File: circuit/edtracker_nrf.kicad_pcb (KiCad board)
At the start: 2 copper layers, 16 parts, among them M1 NRF24LE1_MODULE_SMALL, Q1 TPS1101D, SW1 SW_PUSH_4PIN, U1 NRF24LE1_PROG, U2 MPU-6050, U3 UART_CONN

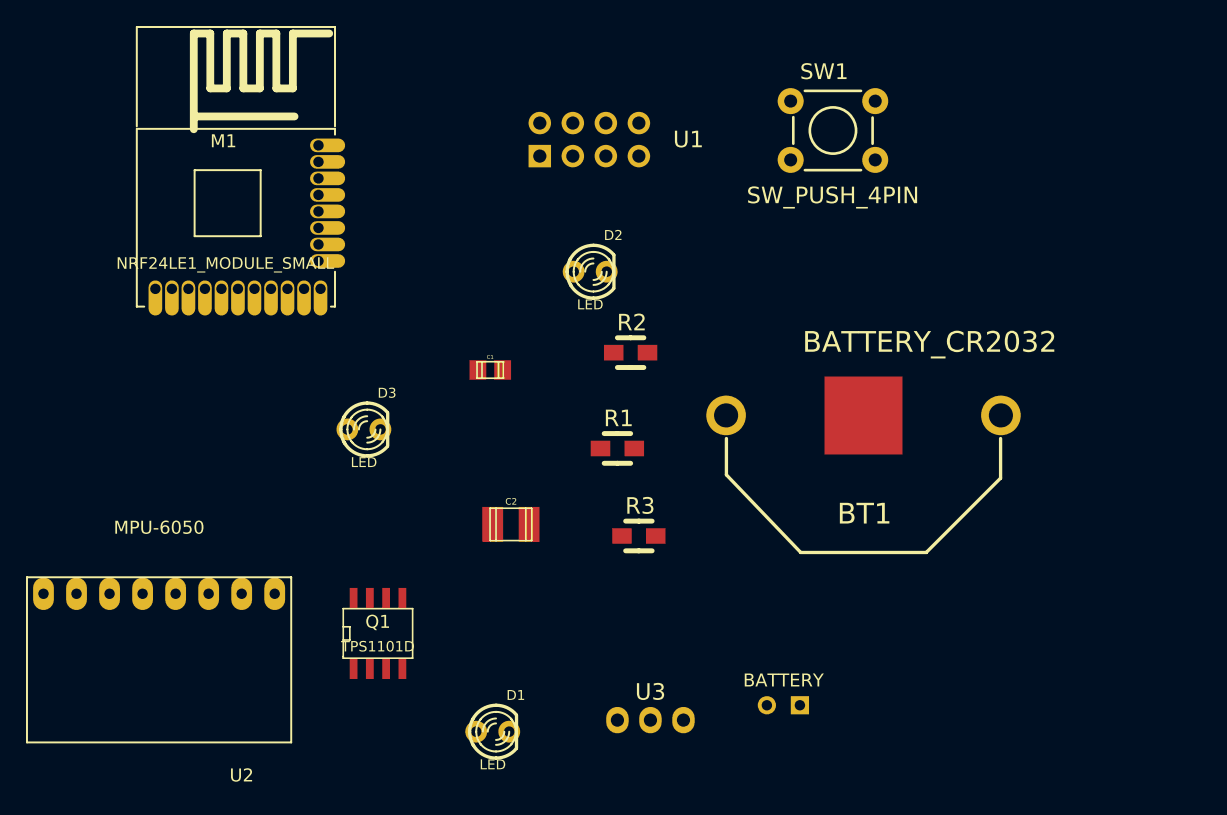
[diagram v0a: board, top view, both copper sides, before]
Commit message: 
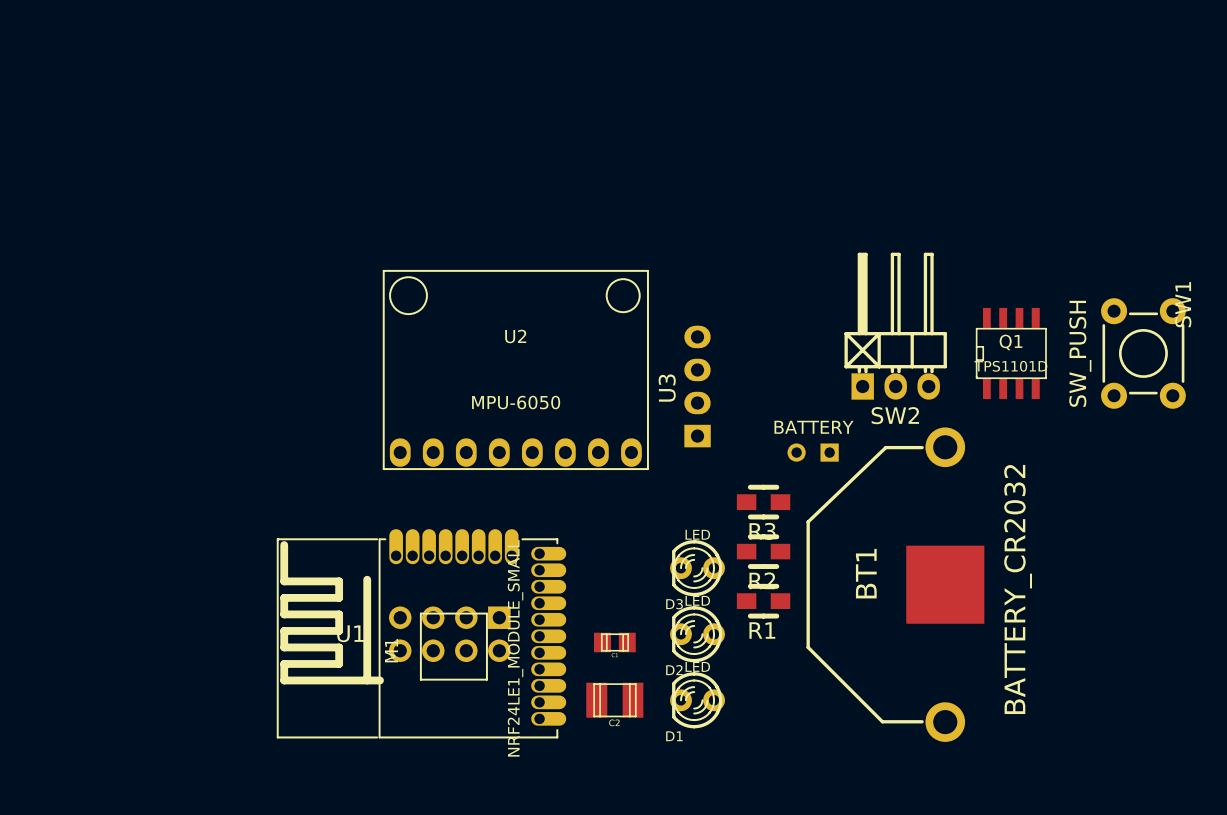
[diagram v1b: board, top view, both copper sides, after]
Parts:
- added SW2: SWITCH_INV, Pin_Headers:Pin_Header_Angled_1x03, F.Cu at (177.8, 100.3)
- SW1: value SW_PUSH_4PIN -> SW_PUSH
- U3: footprint edtracker_nrf:Pin_Header_Angled_1x03 -> edtracker_nrf:Pin_Header_1x04
- moved Q1 53.2 mm to (186.7, 97.8)
- moved U1 39.5 mm to (143.5, 119.4), turned to 180 degrees
- moved M1 36.6 mm to (144.8, 119.4), turned to 90 degrees
- moved U2 35.3 mm to (148.6, 99.1), turned to 180 degrees
- moved SW1 29.4 mm to (196.8, 97.8), turned to 270 degrees
- moved D2 29.1 mm to (162.6, 119.4), turned to 180 degrees
- moved D3 27.8 mm to (162.6, 114.3), turned to 180 degrees
- moved U3 25.9 mm to (162.6, 100.3), turned to 90 degrees
- moved C1 23.0 mm to (156.2, 120.0), turned to 180 degrees
- moved BT2 19.6 mm to (171.4, 105.4)
- moved R2 18.4 mm to (167.6, 113.0), turned to 180 degrees
- moved R1 16.3 mm to (167.6, 116.8), turned to 180 degrees
- moved D1 15.9 mm to (162.6, 124.5), turned to 180 degrees
- moved C2 15.7 mm to (156.2, 124.5), turned to 180 degrees
- moved BT1 14.5 mm to (181.6, 115.6), turned to 270 degrees
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
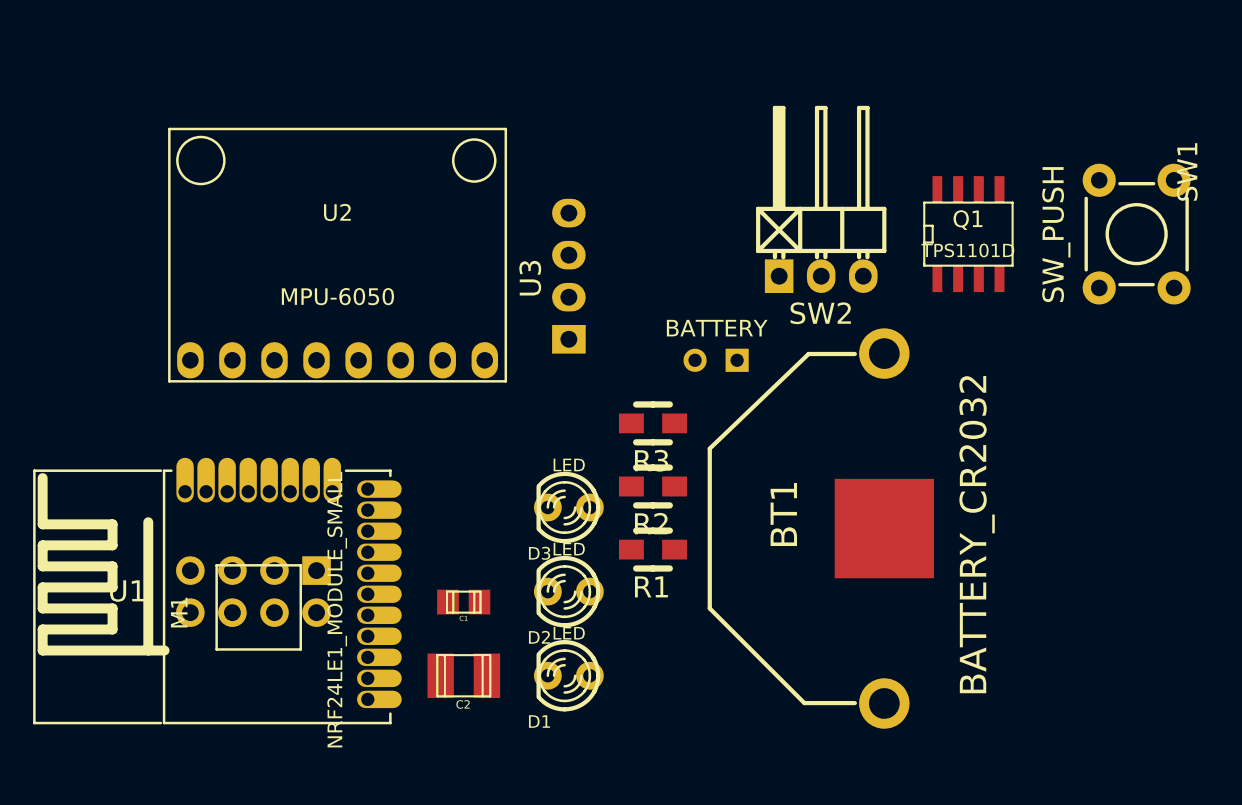
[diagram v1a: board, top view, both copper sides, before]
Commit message: 
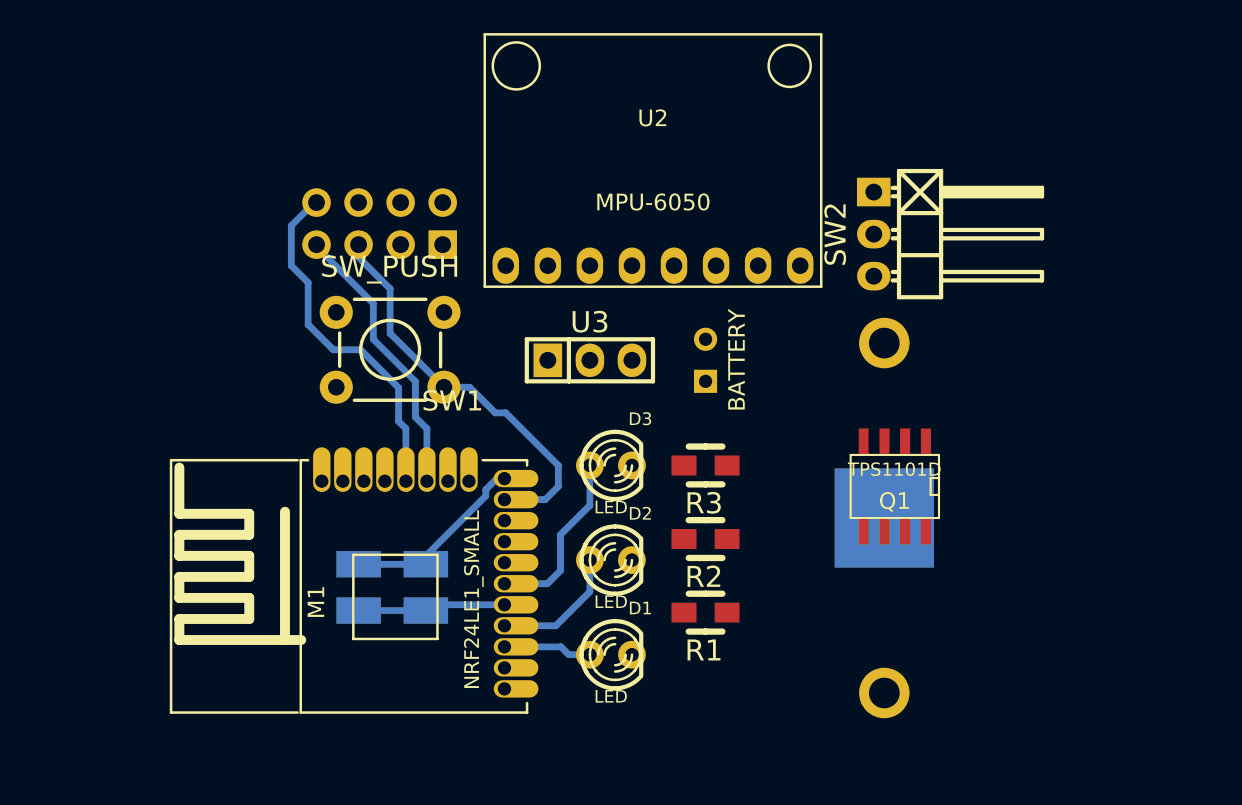
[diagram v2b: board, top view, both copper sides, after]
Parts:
- BT1, C2, U1: moved to B.Cu
- C1: footprint Capacitors_SMD:c_0805 -> Capacitors_SMD:c_1210; moved to B.Cu
- M1: value NRF24LE1_MODULE_SMALL -> NRF24LE1_SMALL
- U3: value UART_CONN -> UART; footprint edtracker_nrf:Pin_Header_1x04 -> edtracker_nrf:Pin_Header_Straight_1x03
- moved SW1 45.6 mm to (151.8, 104.8), turned to 180 degrees
- moved U1 23.5 mm to (151.1, 97.2)
- moved U2 19.9 mm to (167.6, 93.3)
- moved Q1 15.9 mm to (182.2, 113.0), turned to 180 degrees
- moved M1 8.28 mm to (153.0, 118.7)
- moved C1 6.41 mm to (149.9, 119.1), turned to 270 degrees
- moved C2 5.80 mm to (153.9, 119.1), turned to 270 degrees
- moved U3 5.24 mm to (163.8, 105.4), turned to 0 degrees
- moved R1 4.96 mm to (170.8, 120.7)
- moved R2 4.49 mm to (170.8, 116.2)
- moved R3 4.07 mm to (170.8, 111.8)
- moved SW2 4.07 mm to (181.0, 97.8), turned to 270 degrees
- moved D3 3.59 mm to (165.1, 111.8), turned to 0 degrees
- moved D2 3.17 mm to (165.1, 117.5), turned to 0 degrees
- moved D1 2.84 mm to (165.1, 123.2), turned to 0 degrees
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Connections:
- M1 pad 14: /FMOSI -> /FMISO
- U1 pad 7: (no net) -> /FMISO
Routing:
- net /FSCK: track 0.00 -> 24.5 mm
- net /FCSN: track 0.00 -> 21.4 mm
- net /FMISO: track 0.00 -> 17.0 mm
- net GND: track 0.00 -> 11.5 mm
- net Net-(D3-Pad1): track 0.00 -> 10.8 mm
- net VCC: track 0.00 -> 8.96 mm
- net Net-(D2-Pad1): track 0.00 -> 7.92 mm
- net Net-(D1-Pad1): track 0.00 -> 5.36 mm

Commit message: PCB finished, but needs some tweaks
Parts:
- moved Q1 4.06 mm to (178.4, 114.4)
- moved BT1 2.93 mm to (178.8, 114.0)
- moved BT2 0.99 mm to (170.2, 104.6)
- moved U3 0.64 mm to (163.8, 106.0)
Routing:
- net GND: track 11.5 -> 93.9 mm
- net VCC: track 8.96 -> 66.0 mm
- net (no net): track 0.00 -> 50.6 mm
- net Net-(M1-Pad7): track 0.00 -> 44.5 mm
- net Net-(BT1-Pad0): track 0.00 -> 37.0 mm
- net /FMOSI: track 0.00 -> 35.8 mm
- net Net-(M1-Pad12): track 0.00 -> 29.4 mm
- net /SDA: track 0.00 -> 27.6 mm
- net /SCL: track 0.00 -> 22.0 mm
- net Net-(Q1-Pad1): track 0.00 -> 18.5 mm
- net Net-(M1-Pad19): track 0.00 -> 18.4 mm
- net Net-(M1-Pad8): track 0.00 -> 15.0 mm
- net Net-(D1-Pad2): track 0.00 -> 4.20 mm
- net Net-(D2-Pad2): track 0.00 -> 3.67 mm
- net Net-(D3-Pad2): track 0.00 -> 3.14 mm
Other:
- board outline added: 42.7 x 34 mm
- net class Default: clearance 0.254 -> 0.2032
- rule trace_clearance: 0.254 -> 0.2032

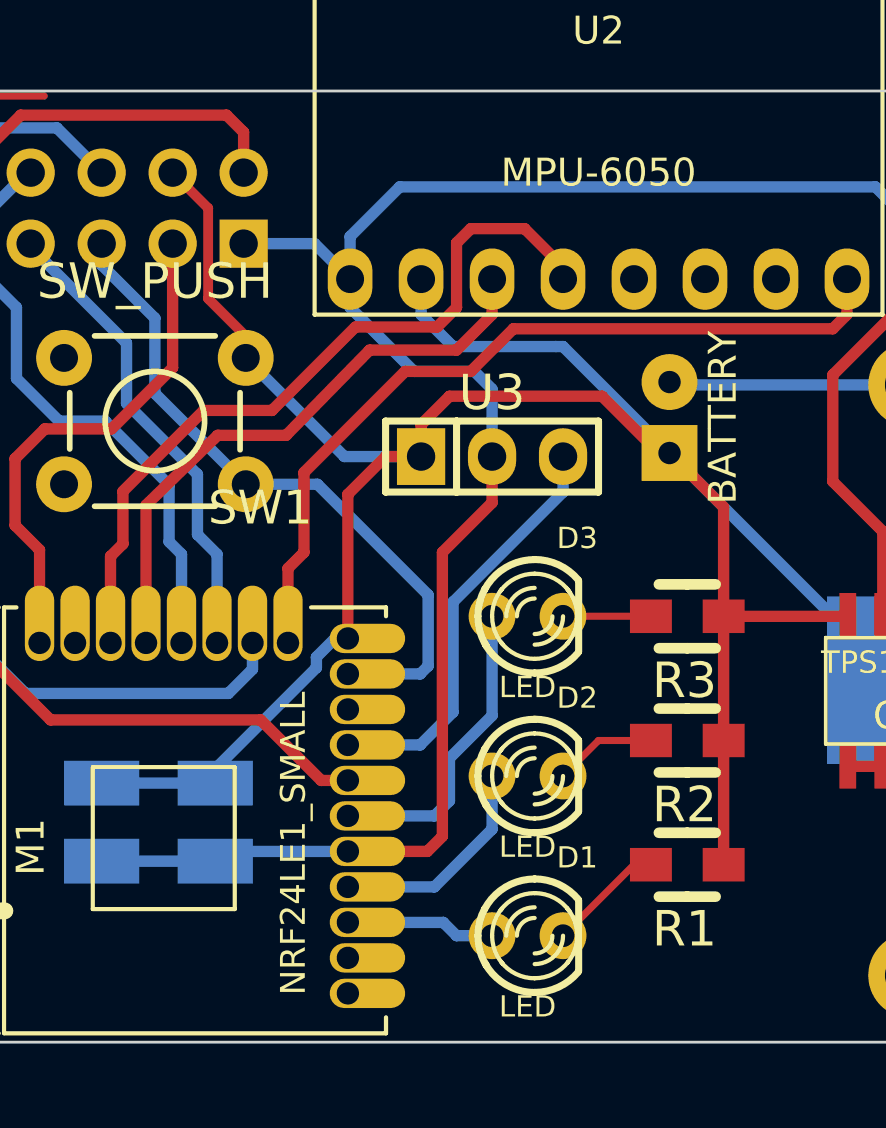
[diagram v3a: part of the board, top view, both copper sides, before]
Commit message: 
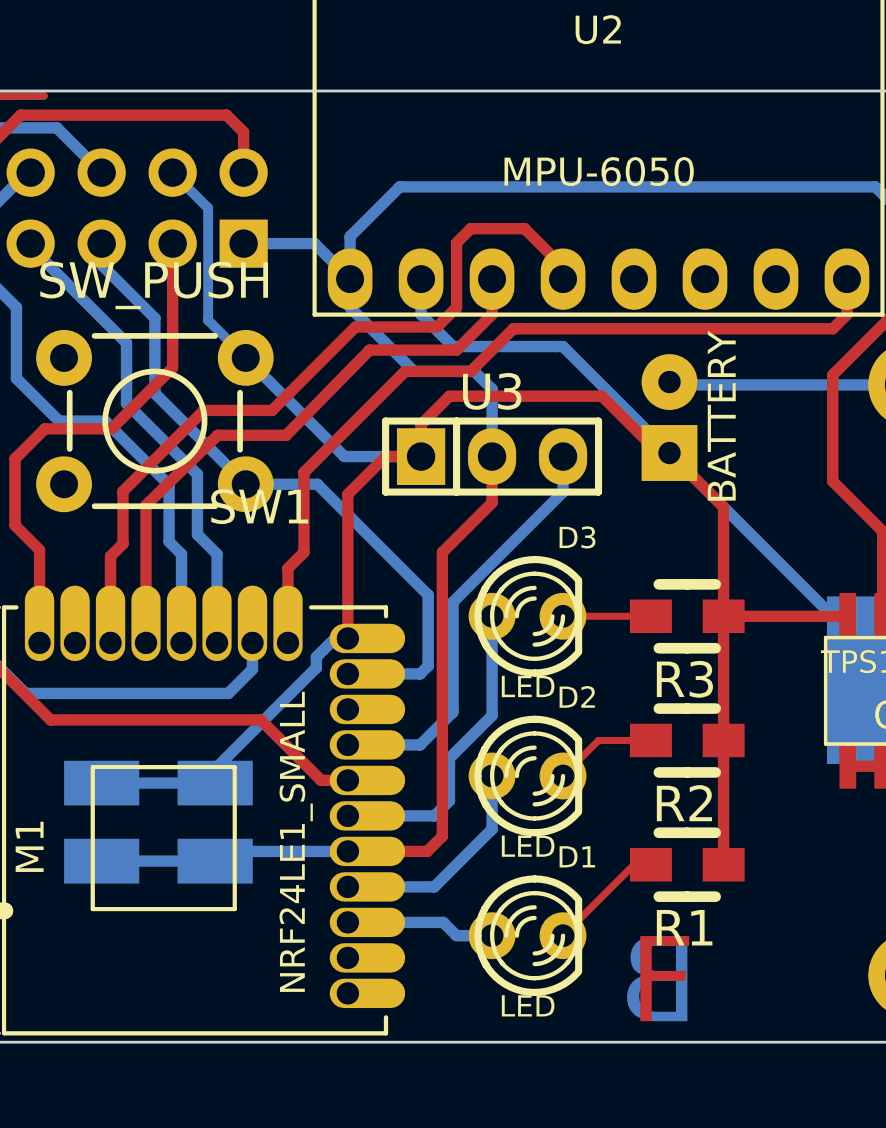
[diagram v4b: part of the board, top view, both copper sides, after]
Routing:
- net GND: track 93.9 -> 94.7 mm
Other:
- board text added: "B"
- board text added: "F"
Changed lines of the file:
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@@
     (links 46)
     (no_connects 2)
-    (area 138.255599 85.394799 191.465201 127.050001)
+    (area 138.255599 85.394799 191.465201 127.2286)
     (thickness 1.6)
-    (drawings 4)
+    (drawings 6)
     (tracks 193)
     (zones 0)
@@
     )
   )
+  (gr_text F (at 169.926 124.841) (layer F.Cu)
+    (effects (font (size 3.048 3.048) (thickness 0.508)))
+  )
+  (gr_text B (at 169.799 124.841) (layer B.Cu)
+    (effects (font (size 3.048 3.048) (thickness 0.508)) (justify mirror))
+  )
   (gr_line (start 143.764 92.964) (end 143.764 127) (angle 90) (layer Edge.Cuts) (width 0.1))
   (gr_line (start 186.436 92.964) (end 143.764 92.964) (angle 90) (layer Edge.Cuts) (width 0.1))
@@
   (segment (start 181.61 114.935) (end 179.07 114.935) (width 0.4064) (layer B.Cu) (net 1) (status 30))
   (segment (start 155.0162 102.5144) (end 155.0162 101.7397) (width 0.3556) (layer F.Cu) (net 1))
-  (segment (start 155.0162 101.7397) (end 153.67 100.3935) (width 0.3556) (layer F.Cu) (net 1))
-  (segment (start 153.67 97.155) (end 152.4 95.885) (width 0.3556) (layer F.Cu) (net 1))
-  (segment (start 153.67 100.3935) (end 153.67 97.155) (width 0.3556) (layer F.Cu) (net 1))
   (segment (start 161.29 106.045) (end 158.5468 106.045) (width 0.4064) (layer B.Cu) (net 1))
   (segment (start 158.5468 106.045) (end 155.0162 102.5144) (width 0.4064) (layer B.Cu) (net 1))
@@
   (segment (start 158.21025 112.55375) (end 158.670625 112.55375) (width 0.4064) (layer B.Cu) (net 1))
   (segment (start 161.29 99.695) (end 161.29 99.06) (width 0.3048) (layer B.Cu) (net 1))
+  (segment (start 153.67 97.155) (end 153.67 101.1682) (width 0.3556) (layer B.Cu) (net 1))
+  (segment (start 153.67 101.1682) (end 155.0162 102.5144) (width 0.3556) (layer B.Cu) (net 1))
+  (segment (start 152.4 95.885) (end 153.67 97.155) (width 0.3556) (layer B.Cu) (net 1))
   (segment (start 178.816 103.4796) (end 179.1716 103.4796) (width 0.4064) (layer F.Cu) (net 2))
   (segment (start 179.1716 103.4796) (end 183.388 107.696) (width 0.4064) (layer F.Cu) (net 2))
